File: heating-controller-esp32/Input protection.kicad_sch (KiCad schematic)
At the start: 2 parts

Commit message: Mounting holes, a few more tweaks
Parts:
- D1: value ~ -> BAS40
- R14: value ~ -> 4.7K
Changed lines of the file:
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@@
       (effects (font (size 1.27 1.27)) (justify left))
     )
-    (property "Value" "~" (id 1) (at 86.6902 70.993 90)
+    (property "Value" "BAS40" (id 1) (at 86.6902 70.993 90)
       (effects (font (size 1.27 1.27)) (justify left))
     )
@@
     (in_bom yes) (on_board yes)
     (property "Reference" "R14" (id 0) (at 101.6 64.5922 90))
-    (property "Value" "~" (id 1) (at 101.6 66.9036 90))
+    (property "Value" "4.7K" (id 1) (at 101.6 66.9036 90))
     (property "Footprint" "Resistor_SMD:R_0603_1608Metric" (id 2) (at 101.6 68.072 90)
       (effects (font (size 1.27 1.27)) hide)

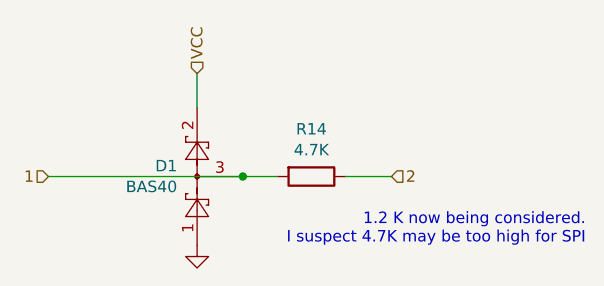
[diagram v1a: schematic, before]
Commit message: Oops. Missing certain files for commit.
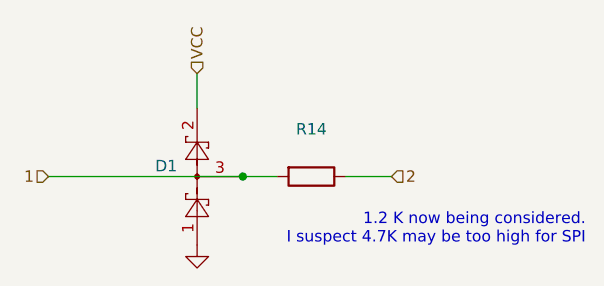
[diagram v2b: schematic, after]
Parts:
- D1: value BAS40 -> ~
- R14: value 4.7K -> ~
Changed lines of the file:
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@@
       (effects (font (size 1.27 1.27)) (justify left))
     )
-    (property "Value" "BAS40" (id 1) (at 86.6902 70.993 90)
+    (property "Value" "~" (id 1) (at 86.6902 70.993 90)
       (effects (font (size 1.27 1.27)) (justify left))
     )
@@
     (in_bom yes) (on_board yes)
     (property "Reference" "R14" (id 0) (at 101.6 64.5922 90))
-    (property "Value" "4.7K" (id 1) (at 101.6 66.9036 90))
+    (property "Value" "~" (id 1) (at 101.6 66.9036 90))
     (property "Footprint" "Resistor_SMD:R_0603_1608Metric" (id 2) (at 101.6 68.072 90)
       (effects (font (size 1.27 1.27)) hide)
